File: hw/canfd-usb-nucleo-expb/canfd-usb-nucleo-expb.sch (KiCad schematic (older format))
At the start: 2 parts, among them J1 Conn_02x19_Odd_Even, J2 Conn_02x19_Odd_Even

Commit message: HW: CAN transceiver with accompanying circuitry was added
CAN transceiver, connectors from nucleo to shiled are added. USB type A for external flash memory also is added.
Signed-off-by: Viacheslav Olizarenko <stiwenss@gmail.com>
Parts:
- removed J1, J2: Conn_02x19_Odd_Even, Pin_Headers:Pin_Header_Straight_2x19_Pitch2.54mm, symbol Connector_Generic:Conn_02x19_Odd_Even
- added C? (x3): 100p, symbol Device:C
- added C? (x3): 4.7n, symbol Device:C
- added C? (x6): 100n, symbol Device:C
- added C? (x3): 15p, symbol Device:C
- added CN10, CN7: Connector_Generic_Conn_02x19_Odd_Even, symbol canfd-usb-nucleo-expb-rescue:Conn_02x19_Odd_Even-canfd-usb-nucleo-expb-cache
- added J? (x3): Conn_01x03, symbol Connector_Generic:Conn_01x03
- added J?: USB_A, symbol Connector:USB_A
- added R? (x11): 62R, symbol Device:R
- added U? (x3): ATA6561-GAQW-N, SOIC8_4P9X3P9MC, symbol canfd-usb-nucleo-expb-rescue:ATA6561-GAQW-N-canfd-usb-nucleo-expb-cache
- added U?: ??, Package_TO_SOT_SMD:SOT-363_SC-70-6, symbol Power_Protection:NUP2202
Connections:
- net labels added: +3.3V, +5V, CAN1_H, CAN1_L, CAN2_H, CAN2_L, CAN3_H, CAN3_L, D+, D-, GND, RX1, RX2, RX3, STANDBY_1, STANDBY_2, STANDBY_3, TX1, TX2, TX3
- wire segments 0 -> 119
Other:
- note added: "+3.3V - ON"
- note added: "Jumper for STANDBY mode\n\n"

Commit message: HW: Schematic edit - buttons and LEDs
Added buttons and LEDs to schematic, minor fixes in
existing components. Assigned most components with
their respective footprints.

Signed-off-by: AlexeyZ <silkt207@gmail.com>
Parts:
- added C16, C17, C18: 100n, Capacitors_SMD:C_0805_HandSoldering, symbol Device:C
- added unit 5 of CN10
- added D1: HEARTBEAT, LEDs:LED_D3.0mm, symbol Device:LED
- added D2: STATUS1, LEDs:LED_D3.0mm, symbol Device:LED
- added D3: STATUS2, LEDs:LED_D3.0mm, symbol Device:LED
- added D4: STATUS3, LEDs:LED_D3.0mm, symbol Device:LED
- added R12, R13, R14, R19: 100k, Resistors_SMD:R_0805_HandSoldering, symbol Device:R
- added R15, R16, R17, R18: 510R, Resistors_SMD:R_0805_HandSoldering, symbol Device:R
- added SW1, SW2, SW3: SW_Push_Dual_x2, Buttons_Switches_THT:SW_PUSH_6mm, symbol Switch:SW_Push_Dual_x2
- C1, C10, C11, C12, C13, C14, C15, C2, C3, C4, C5, C6, C7, C8, C9: renamed from C?; footprint (none) -> Capacitors_SMD:C_0805_HandSoldering
- CN10: value Connector_Generic_Conn_02x19_Odd_Even -> CONN; footprint (none) -> Pin_Headers:Pin_Header_Straight_2x19_Pitch2.54mm; symbol canfd-usb-nucleo-expb-rescue:Conn_02x19_Odd_Even-canfd-usb-nucleo-expb-cache -> canfd-usb-nucleo:Conn_02x19_Odd_Even
- CN7: value Connector_Generic_Conn_02x19_Odd_Even -> POWER; footprint (none) -> Pin_Headers:Pin_Header_Straight_2x19_Pitch2.54mm; symbol canfd-usb-nucleo-expb-rescue:Conn_02x19_Odd_Even-canfd-usb-nucleo-expb-cache -> canfd-usb-nucleo:Conn_02x19_Odd_Even
- J1: renamed from J?; symbol Connector:USB_A -> Connector:USB_B_Mini
- J3, J4, J5: renamed from J?; footprint (none) -> Pin_Headers:Pin_Header_Straight_1x03_Pitch2.54mm
- R1, R10, R11, R2, R3, R4, R5, R6, R7, R8, R9: renamed from R?; footprint (none) -> Resistors_SMD:R_0805_HandSoldering
- U2, U3, U4: renamed from U?; footprint SOIC8_4P9X3P9MC -> Housings_SOIC:SOIC-8_3.9x4.9mm_Pitch1.27mm; symbol canfd-usb-nucleo-expb-rescue:ATA6561-GAQW-N-canfd-usb-nucleo-expb-cache -> canfd-usb-nucleo:ATA6561-GAQW-N
- gave numbers to parts that had none: 1
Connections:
- net labels added: LED1, LED2, LED3, LED4, SW1, SW2, SW3
- wire segments 119 -> 166
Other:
- moved on the sheet: C1, C10, C11, C12, C13, C14, C15, C2, C3, C4, C5, C6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

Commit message: HW: Schematic update - BH connectors
1. Added BH connectors for ribbon cable connection to CAN-bus.
2. Hopefuly fixed the kicad library linking problem.
Schematic is ready to be reviewed before
laying out the PCB.

Signed-off-by: AlexeyZ <silkt207@gmail.com>
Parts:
- added D?: D_Schottky, symbol Device:D_Schottky
- added J? (x3): Conn_01x10, symbol canfd-usb-nucleo:BH_Conn_01x10
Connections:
- wire segments 166 -> 200
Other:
- moved on the sheet: C1, C10, C11, C12, C13, C14, C15, C16, C17, C18, C2, C3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

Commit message: HW: Schematic fixes, PCB outline fixes
1. PCB outline is now a rectangle, arduino pins are removed
2. 22u tantalum cap added on 5V rail
3. USB termination resistors are removed as they are implemented
in MCU's PHY
4. Buttons are stronger pulled-up with 10k resistors instead of
100k like on other stm boards, 100 Ohm resistors added in series
with debouncing caps
5.Placeholder components remowed
6.Shielding through 220k resistor with 10n cap
7.ESD protection connection fixed
8.USB Type-C instead of Mini-B
9. Replaced standby mode jumpers with solder-jumpers for choosing
between always normal mode or controlled through MCU. Current-limiting
resistors added on standby lines.

Co-authored-by: Viacheslav Olizarenko <stiwenss@gmail.com>
Co-authored-by: AlexeyZ <silkt207@gmail.com>
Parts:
- removed C10, C11, C12: 100p, Capacitors_SMD:C_0805_HandSoldering, symbol Device:C
- removed C4, C5, C6: 15p, Capacitors_SMD:C_0805_HandSoldering, symbol Device:C
- removed J1: USB_A, symbol Connector:USB_B_Mini
- removed J3, J4, J5: Conn_01x03, Pin_Headers:Pin_Header_Straight_1x03_Pitch2.54mm, symbol Connector_Generic:Conn_01x03
- removed R1, R2, R3, R4, R5: 62R, Resistors_SMD:R_0805_HandSoldering, symbol Device:R
- removed R12: 100k, Resistors_SMD:R_0805_HandSoldering, symbol Device:R
- removed U1: ??, Package_TO_SOT_SMD:SOT-363_SC-70-6, symbol Power_Protection:NUP2202
- added C?: 2.2u, Capacitors_SMD:C_0805_HandSoldering, symbol Device:C
- added C?: 10nf, Capacitors_SMD:C_0805_HandSoldering, symbol Device:C
- added C?: 22u, Capacitors_SMD:C_0805_HandSoldering, symbol Device:CP
- added J?: USB_C_Receptacle_USB2.0, symbol Connector:USB_C_Receptacle_USB2.0
- added JP? (x6): Jumper_2_Open, symbol Jumper:Jumper_2_Open
- added R?: 220k, Resistors_SMD:R_0805_HandSoldering, symbol Device:R
- added R? (x3): 1k, Resistors_SMD:R_0805_HandSoldering, symbol Device:R
- added R? (x3): 100R, Resistors_SMD:R_0805_HandSoldering, symbol Device:R
- added U?: USBLC6-2SC6, Package_TO_SOT_SMD:SOT-363_SC-70-6, symbol Power_Protection:NUP2202
- R13, R14, R19: value 100k -> 10k
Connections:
- wire segments 200 -> 205
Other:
- note added: "Solder jumper or 0R resistor\nfor STANDBY mode"
- note removed: "+3.3V - ON"
- note removed: "Jumper for STANDBY mode\n\n"
- moved on the sheet: C2, CN10C, CN10E, CN7D, D?

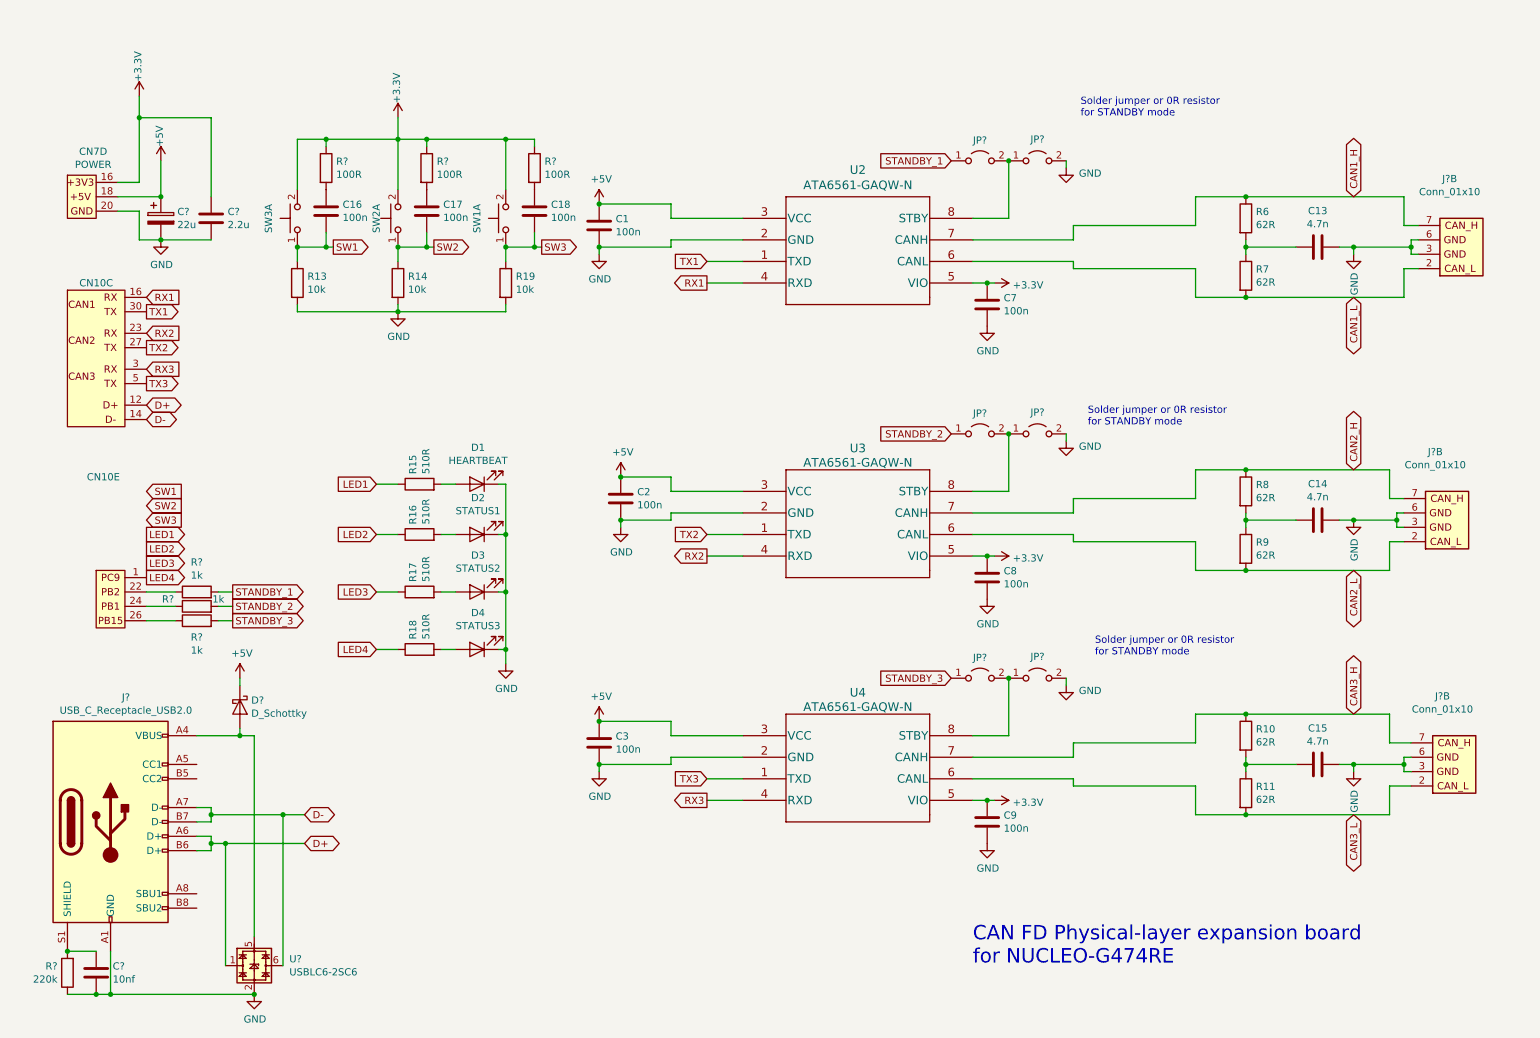
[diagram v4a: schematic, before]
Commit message: HW: Added footprints for all components
Created the footprint for USB-Type-C connector
Added footprints for the rest of the components on the PCB.
Started the mock-up placement of components on the board

Signed-off-by: AlexeyZ <silkt207@gmail.com>
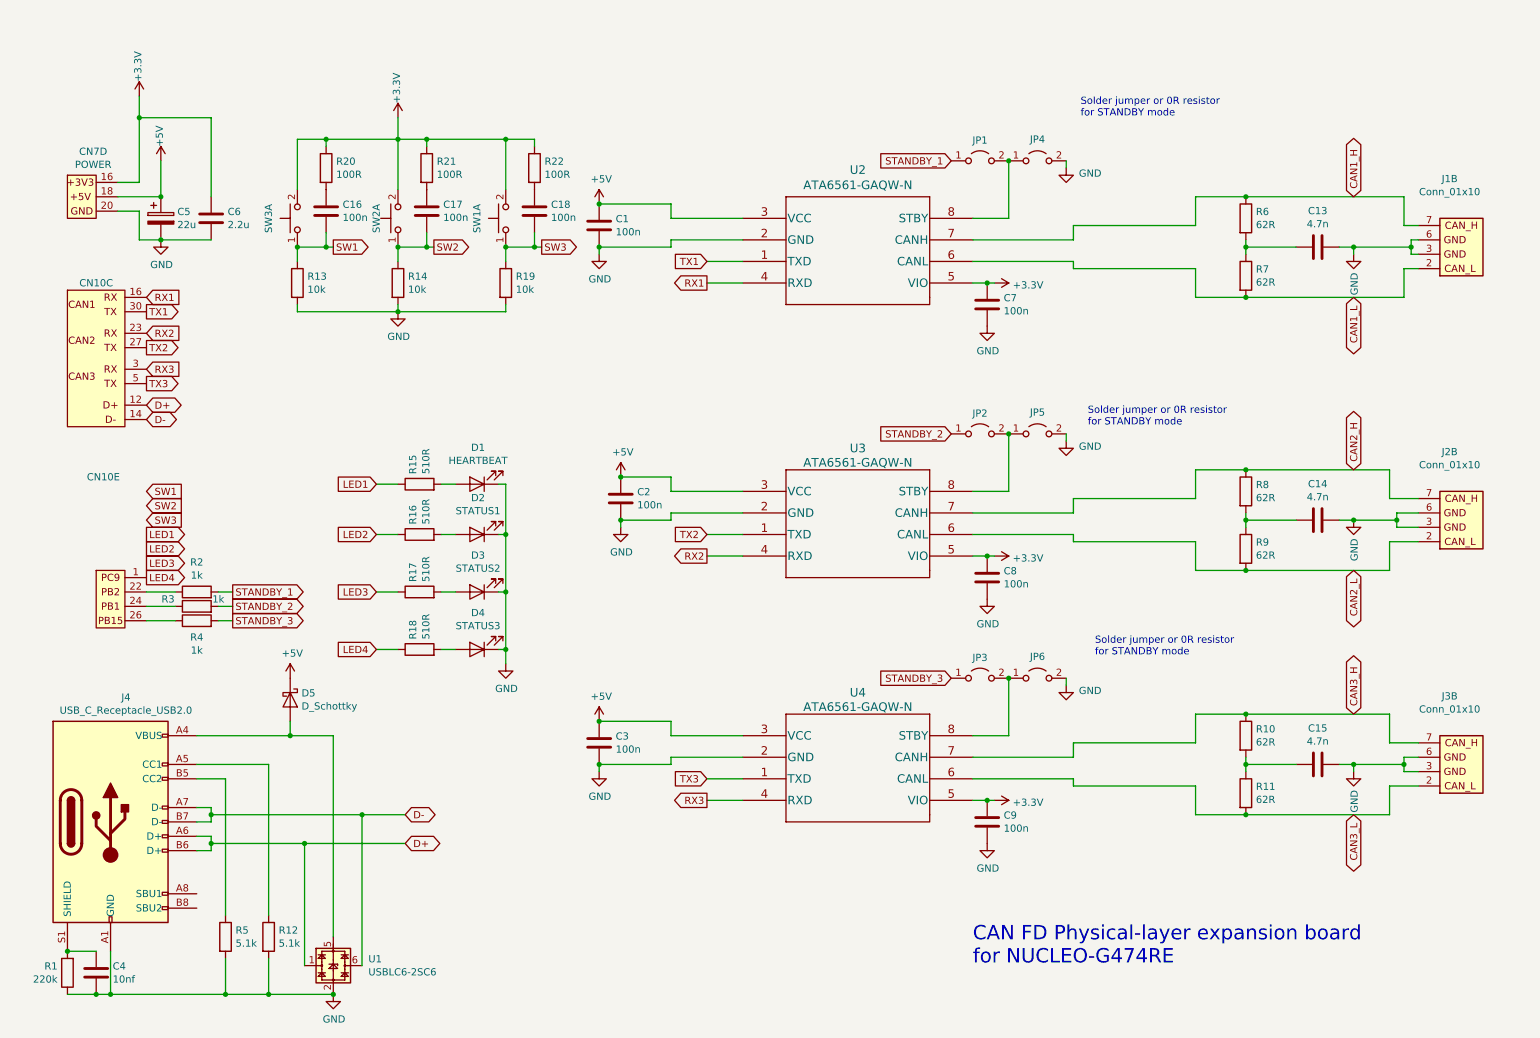
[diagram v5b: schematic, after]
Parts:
- added R12, R5: 5.1k, Resistors_SMD:R_0805_HandSoldering, symbol Device:R
- D5: renamed from D?; footprint (none) -> Diodes_SMD:D_SOD-123
- J1, J2, J3: renamed from J?; footprint (none) -> can-usb:IDC-Header_2x05_P2.54mm_Vertical
- J4: renamed from J?; footprint (none) -> can-usb:L-KLS1-TIPEC-B
- JP1, JP2, JP3, JP4, JP5, JP6: renamed from JP?; footprint (none) -> can-usb:SolderJumper-2_P1.3mm_Open_RoundedPad1.0x1.5mm
- U1: renamed from U?; footprint Package_TO_SOT_SMD:SOT-363_SC-70-6 -> TO_SOT_Packages_SMD:SOT-23-6_Handsoldering
- gave numbers to parts that had none: 10
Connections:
- net GND: now also R12.2, R5.2
- net at J4.A5 (CC1): now also R12.1
- net at J4.B5 (CC2): now also R5.1
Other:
- moved on the sheet: D5, J2B, J3B, U1

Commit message: HW: Footprints and components layout
Added footprints for all components and created a new one for USB
connector. Started the components layout with positioning of all
components on the PCB before laying out the traces.

Signed-off-by: AlexeyZ <silkt207@gmail.com>
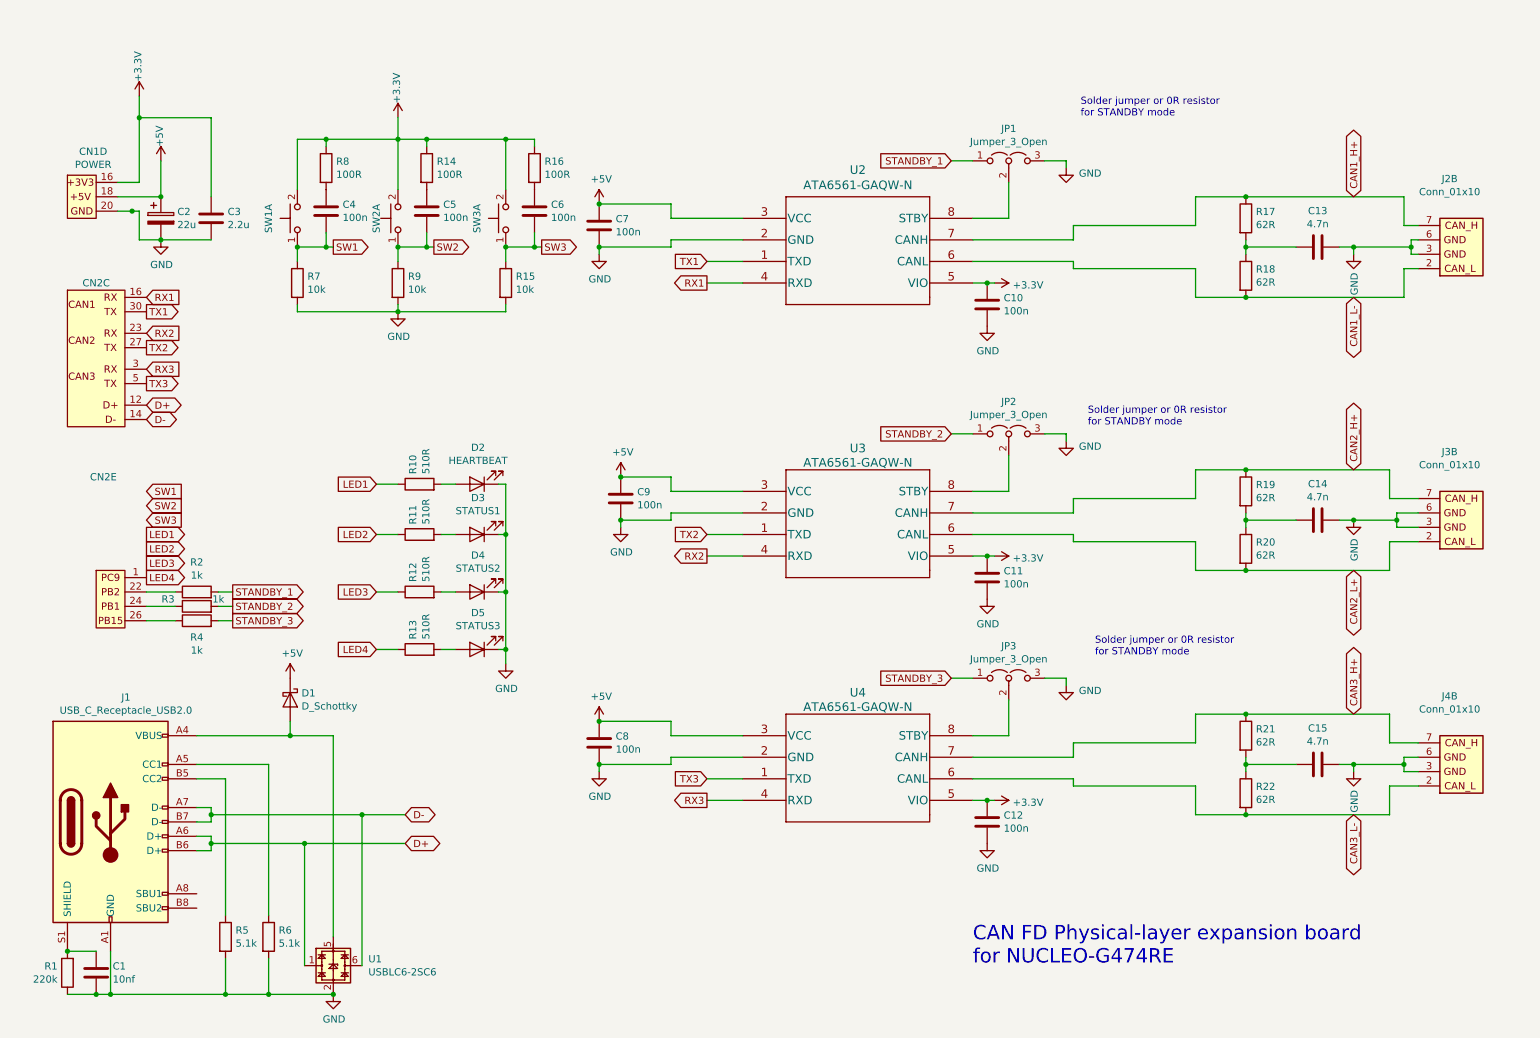
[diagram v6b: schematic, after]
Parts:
- removed JP1, JP2, JP3, JP4, JP5, JP6: Jumper_2_Open, can-usb:SolderJumper-2_P1.3mm_Open_RoundedPad1.0x1.5mm, symbol Jumper:Jumper_2_Open
- added JP1, JP2, JP3: Jumper_3_Open, can-usb:SolderJumper-3_P1.3mm_Open_RoundedPad1.0x1.5mm, symbol Jumper:Jumper_3_Open
- SW1: renamed from SW3; footprint Buttons_Switches_THT:SW_PUSH_6mm -> Button_Switch_THT:SW_PUSH_6mm
- SW2: footprint Buttons_Switches_THT:SW_PUSH_6mm -> Button_Switch_THT:SW_PUSH_6mm
- SW3: renamed from SW1; footprint Buttons_Switches_THT:SW_PUSH_6mm -> Button_Switch_THT:SW_PUSH_6mm
- renumbered C4 to C1, C7 to C10, C8 to C11, C9 to C12, C5 to C2, C6 to C3, C16 to C4, C17 to C5, C18 to C6, C1 to C7, C3 to C8, C2 to C9, CN7 to CN1, CN10 to CN2, D5 to D1, D1 to D2, D2 to D3, D3 to D4, D4 to D5, J4 to J1, J1 to J2, J2 to J3, J3 to J4, R15 to R10, R16 to R11, R17 to R12, R18 to R13, R21 to R14, R19 to R15, R22 to R16, R6 to R17, R7 to R18, R8 to R19, R9 to R20, R10 to R21, R11 to R22, R12 to R6, R13 to R7, R20 to R8, R14 to R9
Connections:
- net GND: now also JP1.3 (B), JP2.3 (B), JP3.3 (B)
- net STANDBY_1: now also JP1.1 (A)
- net STANDBY_2: now also JP2.1 (A)
- net STANDBY_3: now also JP3.1 (A)
- net at U2.8 (STBY): now also JP1.2 (C)
- net at U3.8 (STBY): now also JP2.2 (C)
- net at U4.8 (STBY): now also JP3.2 (C)
- net CAN1_H renamed CAN1_H+
- net CAN1_L renamed CAN1_L-
- net CAN2_H renamed CAN2_H+
- net CAN2_L renamed CAN2_L+
- net CAN3_H renamed CAN3_H+
- net CAN3_L renamed CAN3_L-

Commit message: HW: PCB Layout: Part 1
Fixed the USBLC6-2SC6 part;
Routed most of the PHY can parts of the board.

Signed-off-by: AlexeyZ <silkt207@gmail.com>
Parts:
- U1: symbol Power_Protection:NUP2202 -> canfd-usb-nucleo:NUP2202
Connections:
- net D+: now also U1.6 (io1)
- net D-: now also U1.3, U1.4; no longer U1.6
- net RX2: now also CN2.3 (rx3); no longer CN2.23 (Pin_30)
- net RX3: now also CN2.23 (Pin_30); no longer CN2.3 (rx3)
- net TX2: now also CN2.5 (tx3); no longer CN2.27 (Pin_30)
- net TX3: now also CN2.27 (Pin_30); no longer CN2.5 (tx3)
- net CAN1_H+ renamed CAN1_P
- net CAN1_L- renamed CAN1_N
- net CAN2_H+ renamed CAN2_P
- net CAN2_L+ renamed CAN2_N
- net CAN3_H+ renamed CAN3_P
- net CAN3_L- renamed CAN3_N
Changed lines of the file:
@@
 	8650 2100 8650 2300
 Text GLabel 9750 2300 3    50   BiDi ~ 0
-CAN1_L-
+CAN1_N
 Text GLabel 9750 1600 1    50   BiDi ~ 0
-CAN1_H+
+CAN1_P
 $Comp
 L power:+3.3V #PWR018
@@
 TX1
 Text GLabel 1350 2550 2    50   Input ~ 0
+RX3
+Text GLabel 1350 2650 2    50   Output ~ 0
+TX3
+Text GLabel 1350 2800 2    50   Input ~ 0
 RX2
-Text GLabel 1350 2650 2    50   Output ~ 0
+Text GLabel 1350 2900 2    50   Output ~ 0
 TX2
-Text GLabel 1350 2800 2    50   Input ~ 0
-RX3
-Text GLabel 1350 2900 2    50   Output ~ 0
-TX3
 Text GLabel 1350 3150 2    50   BiDi ~ 0
 D-
@@
 	8650 4000 8650 4200
 Text GLabel 9750 4200 3    50   BiDi ~ 0
-CAN2_L+
+CAN2_N
 Text GLabel 9750 3500 1    50   BiDi ~ 0
-CAN2_H+
+CAN2_P
 $Comp
 L power:+3.3V #PWR019
@@
 	8650 5700 8650 5900
 Text GLabel 9750 5900 3    50   BiDi ~ 0
-CAN3_L-
+CAN3_N
 Text GLabel 9750 5200 1    50   BiDi ~ 0
-CAN3_H+
+CAN3_P
 $Comp
 L power:+3.3V #PWR020
@@
 Wire Wire Line
 	5250 5650 5500 5650
-Wire Wire Line
-	1150 1700 1250 1700
 $Comp
 L power:+3.3V #PWR01
@@
 	1700 6150 1800 6150
 Wire Wire Line
-	1800 5850 1800 5900
-Wire Wire Line
 	1800 6050 1800 6100
-Connection ~ 1800 5900
-Wire Wire Line
-	1800 5900 1800 5950
 Connection ~ 1800 6100
 Wire Wire Line
@@
 Wire Wire Line
 	2200 7150 2650 7150
-Wire Wire Line
-	2850 6950 2850 5900
-Connection ~ 2850 5900
-Wire Wire Line
-	1800 5900 2850 5900
-Wire Wire Line
-	2850 5900 3150 5900
 $Comp
 L Device:R R6
@@
 $EndComp
 $Comp
-L Power_Protection:NUP2202 U1
+L canfd-usb-nucleo:NUP2202 U1
 U 1 1 5E775B10
 P 2650 6950
@@
 Wire Wire Line
 	7100 4950 6950 4950
-Connection ~ 1250 1700
-Wire Wire Line
-	1250 1700 1300 1700
 $Comp
 L Device:R R20
@@
 	1    0    0    -1
 $EndComp
+Wire Wire Line
+	1150 1700 1300 1700
+Wire Wire Line
+	1800 5850 1800 5900
+Connection ~ 1800 5900
+Wire Wire Line
+	1800 5900 1800 5950
+Wire Wire Line
+	2850 6950 2850 5900
+Wire Wire Line
+	1800 5900 2850 5900
+Connection ~ 2850 5900
+Wire Wire Line
+	2850 5900 3150 5900
 $EndSCHEMATC
